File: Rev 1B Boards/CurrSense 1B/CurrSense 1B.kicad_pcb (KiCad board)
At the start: 4 copper layers, 135.8 x 56 mm, 52 parts, among them J1 Conn_01x01_Pin, J10 Conn_01x01_Pin, J13 Banana 2P, J14 Banana 2P, J15 Banana 2P, J2 Conn_01x01_Pin, J3 XT30_F, J4 Banana 2P, J5 Banana 2P, J6 XT30_F, J7 XT30_F, J8 Banana 2P, J9 XT30_F, Q1 BSC059N04LS6, Q2 BSC059N04LS6, U1 MAX4073T, U2 OPA551U, U3 TLV9301xDBV, U4 OPA551U, U5 TLV9301xDBV

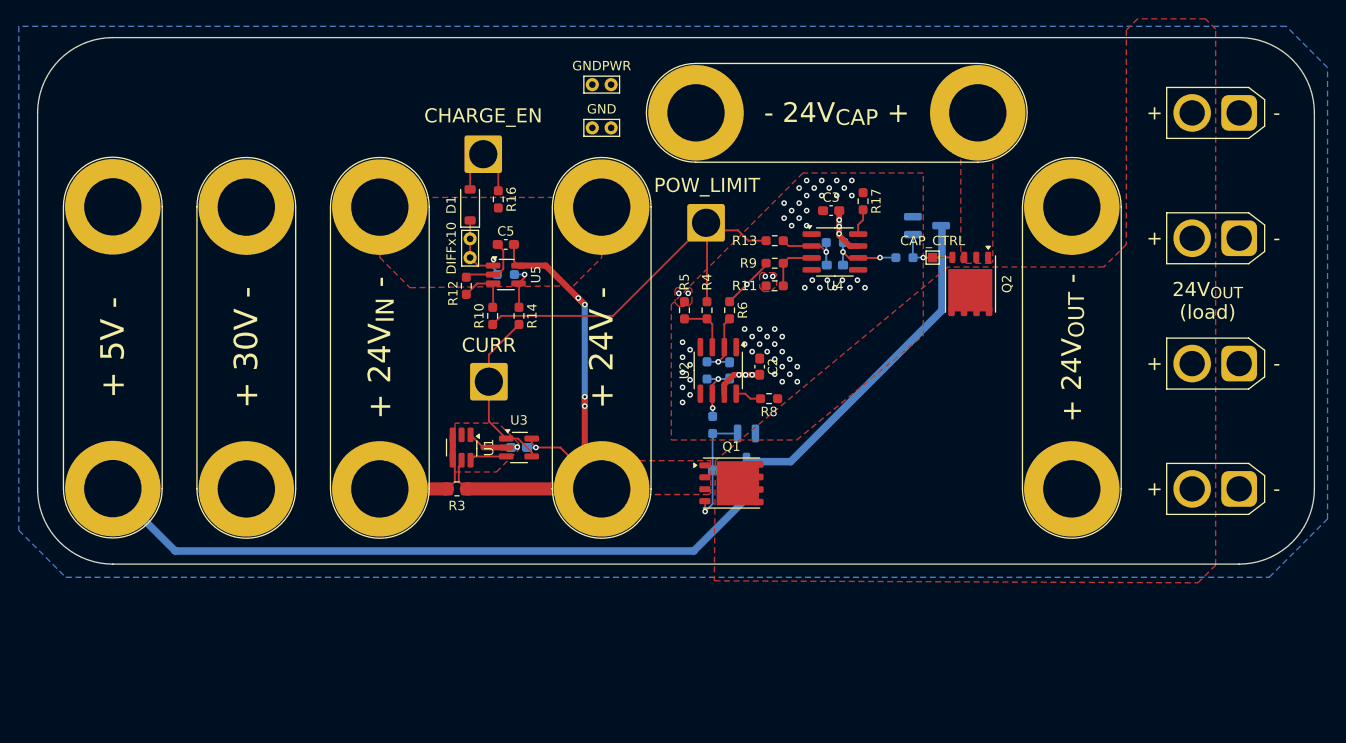
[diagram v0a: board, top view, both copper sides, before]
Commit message: Adjust all PCBs and resize boards to be cheaper to order from JLCPCB
Also changed connector pinout to reflect silkscreen
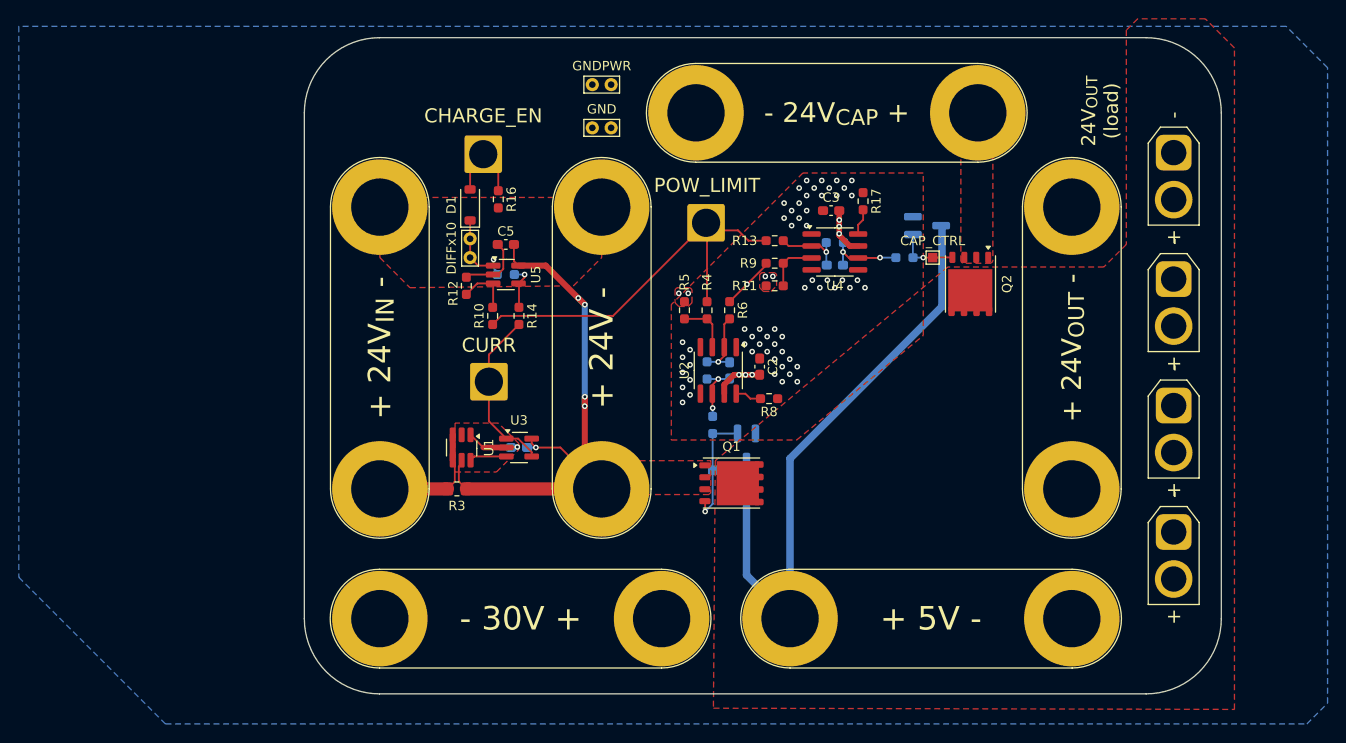
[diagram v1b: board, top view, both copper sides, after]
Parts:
- moved J15 73.3 mm to (159.2, 129.0), turned to 0 degrees
- moved J13 46.3 mm to (145.6, 129.0), turned to 180 degrees
- moved J3 8.34 mm to (200.0, 119.8), turned to -90 degrees
- moved J6 8.27 mm to (200.0, 106.3), turned to -90 degrees
- moved J7 8.21 mm to (200.0, 92.9), turned to -90 degrees
- moved J9 8.15 mm to (200.0, 79.4), turned to -90 degrees
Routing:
- net +5V: track 112.9 -> 67.2 mm
- net VCC: track 115.5 -> 93.1 mm
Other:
- board size 135.8 x 56 mm -> 97.5 x 69.8 mm
- board text added: "- 30V +"
- board text removed: "+ 30V -"

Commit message: Replace most banana jacks with XT connectors
+ update library
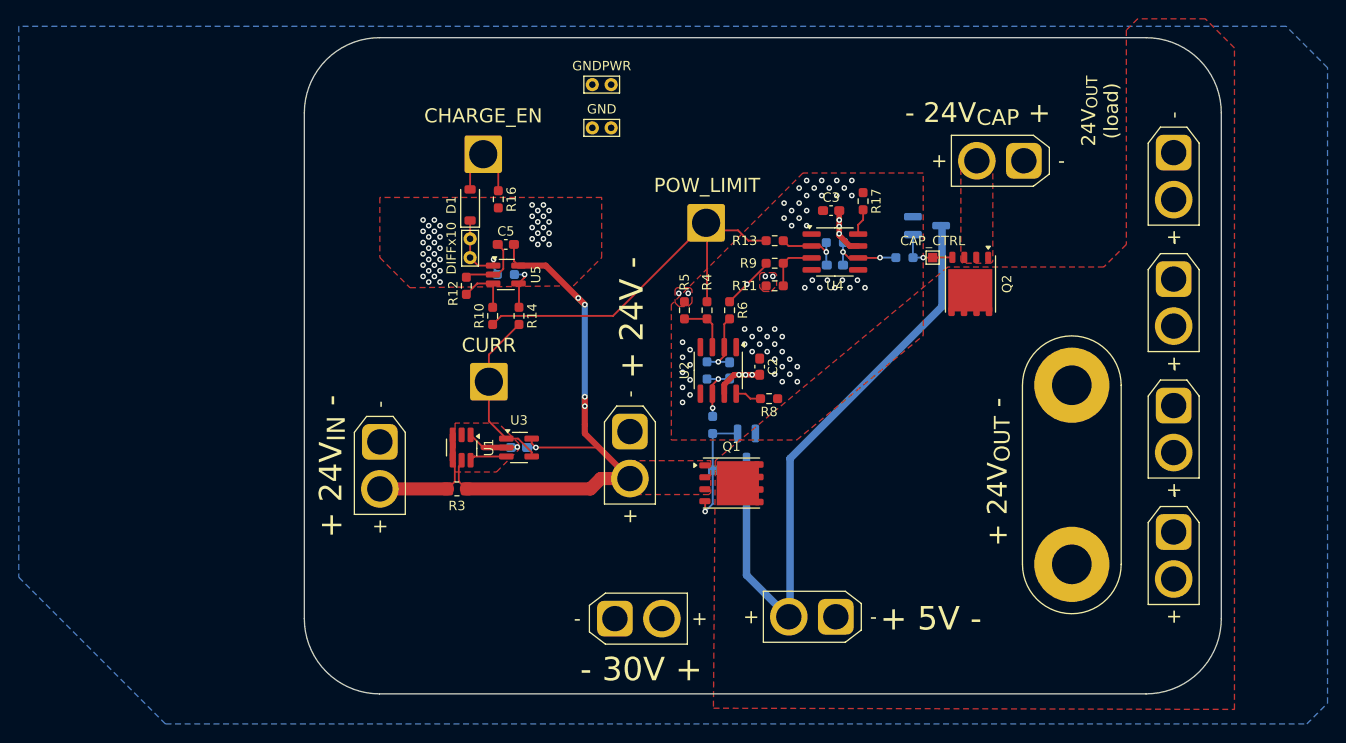
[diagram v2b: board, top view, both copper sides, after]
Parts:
- removed J4, J5, J8: Banana 2P, Connector:Banana_Jack_2Pin
- added J11: XT30_F, Connector_AMASS:AMASS_XT30U-F_1x02_P5.0mm_Vertical, F.Cu at (140.6, 129.0)
- added J12: XT30_F, Connector_AMASS:AMASS_XT30U-F_1x02_P5.0mm_Vertical, F.Cu at (164.1, 128.8)
- added J16: Banana, ! Robomaster Connectors:RM_Banana_Jack_2Pin, F.Cu at (189.2, 123.2)
- J13, J14, J15: value Banana 2P -> XT30_F; footprint Connector:Banana_Jack_2Pin -> Connector_AMASS:AMASS_XT30U-F_1x02_P5.0mm_Vertical
- moved J15 47.5 mm to (115.6, 110.2), turned to -90 degrees
- moved J13 20.2 mm to (142.2, 109.1), turned to -90 degrees
- moved J14 7.07 mm to (184.1, 80.3)
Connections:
- J13 pad 1: VCC -> GNDPWR
- J13 pad 2: GND -> +24V
- J14 pad 1: /+24V_CAP_IN -> GNDPWR
- J14 pad 2: GNDPWR -> /+24V_CAP_IN
- J15 pad 1: +5V -> GNDPWR
- J15 pad 2: GNDPWR -> /+24_IN
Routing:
- net +24V: track 62.4 -> 68.5 mm
- net GNDPWR: vias 5 -> 45

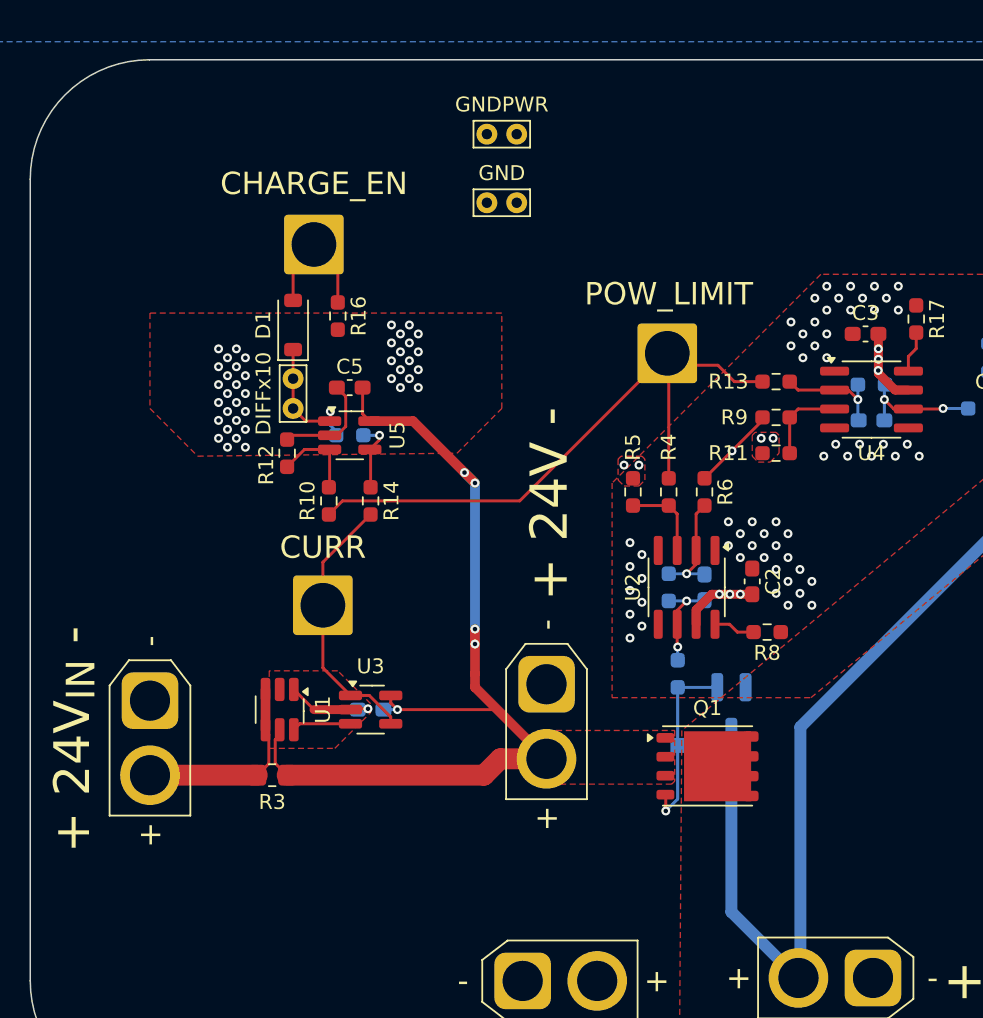
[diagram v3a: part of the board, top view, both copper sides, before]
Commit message: added test points to current sense PCB
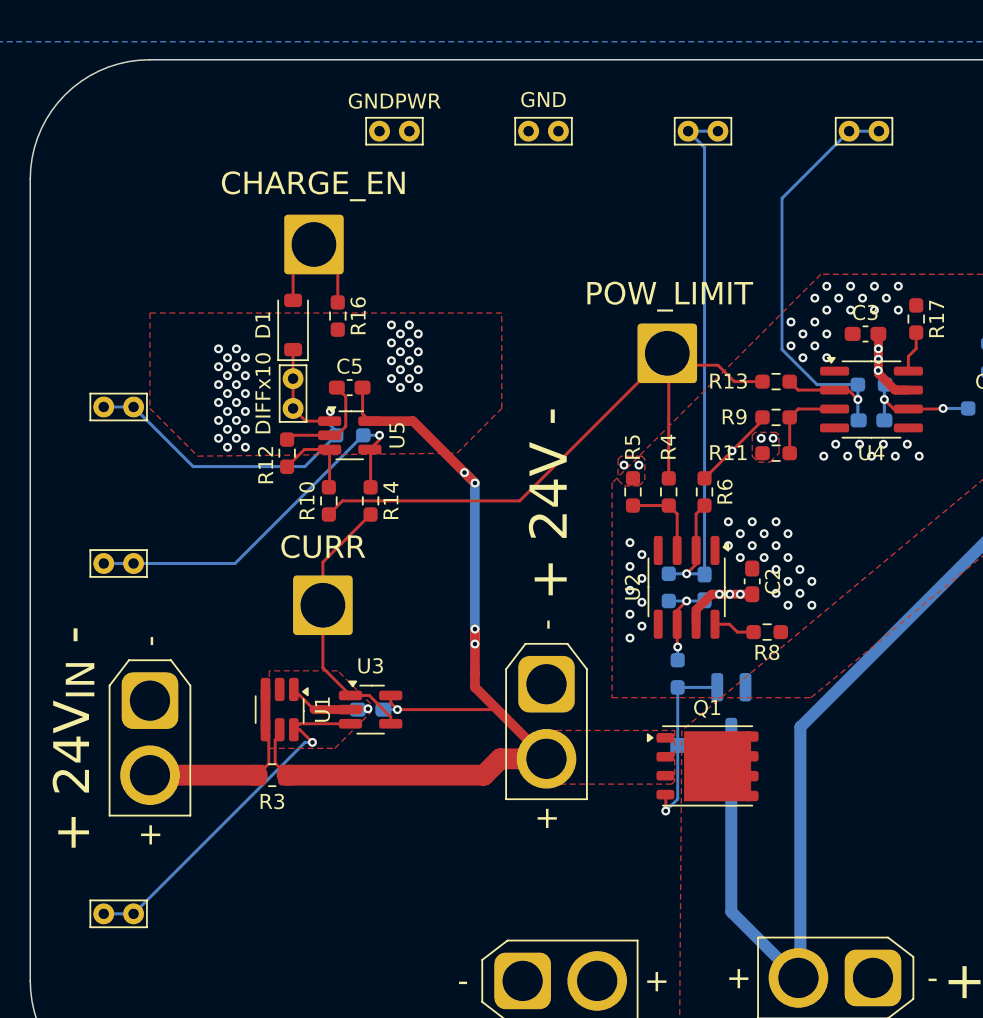
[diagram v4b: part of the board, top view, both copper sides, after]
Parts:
- added TP10: BAT_IN_NEG, TestPoint:TestPoint_Bridge_Pitch2.0mm_Drill0.7mm, F.Cu at (153.7, 72.0)
- added TP6: CE_OUT, TestPoint:TestPoint_Bridge_Pitch2.0mm_Drill0.7mm, F.Cu at (114.5, 90.5)
- added TP7: CE_IN_NEG, TestPoint:TestPoint_Bridge_Pitch2.0mm_Drill0.7mm, F.Cu at (114.5, 101.0)
- added TP8: I_OUT, TestPoint:TestPoint_Bridge_Pitch2.0mm_Drill0.7mm, F.Cu at (114.5, 124.5)
- added TP9: CAP_IN_NEG, TestPoint:TestPoint_Bridge_Pitch2.0mm_Drill0.7mm, F.Cu at (164.5, 72.0)
- moved TP3 7.20 mm to (131.0, 72.0)
- moved TP2 5.56 mm to (141.0, 72.0)
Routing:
- net /Current Sense/1-: track 7.49 -> 39.7 mm
- net /Current Sense/2-: track 7.49 -> 32.1 mm
- net /Current Sense/3-: track 4.86 -> 25.8 mm
- net /Current Sense/CURR_{RAW}: track 3.97 -> 24.3 mm, vias 0 -> 1
- net /Current Sense/DIFF10: track 9.18 -> 27.3 mm
